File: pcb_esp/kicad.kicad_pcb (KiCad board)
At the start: 2 copper layers, 100 x 30 mm, 26 parts, among them J1 PRG, J2 SLP, J3 SHT21, J4 BH1750, J5 PWRIN, J6 GND, SW1 RST, SW2 PRG, U1 LT1963, U2 ESP-12F

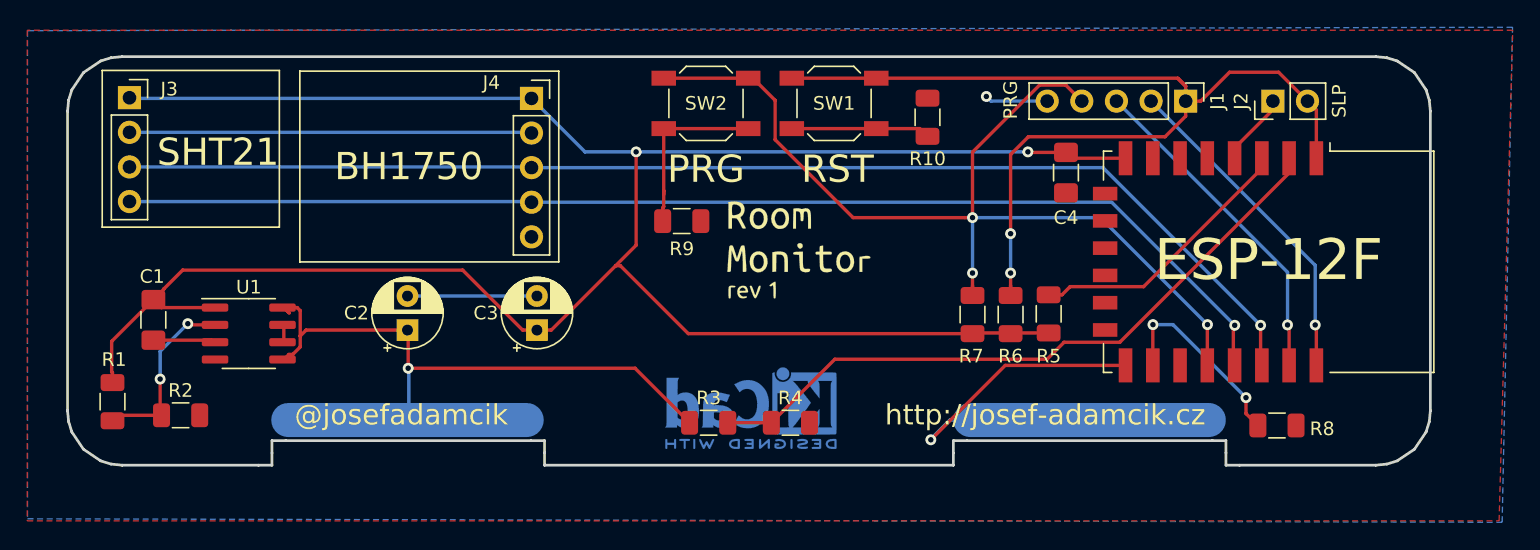
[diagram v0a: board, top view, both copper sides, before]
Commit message: Add GND connecting vias to the main PCB
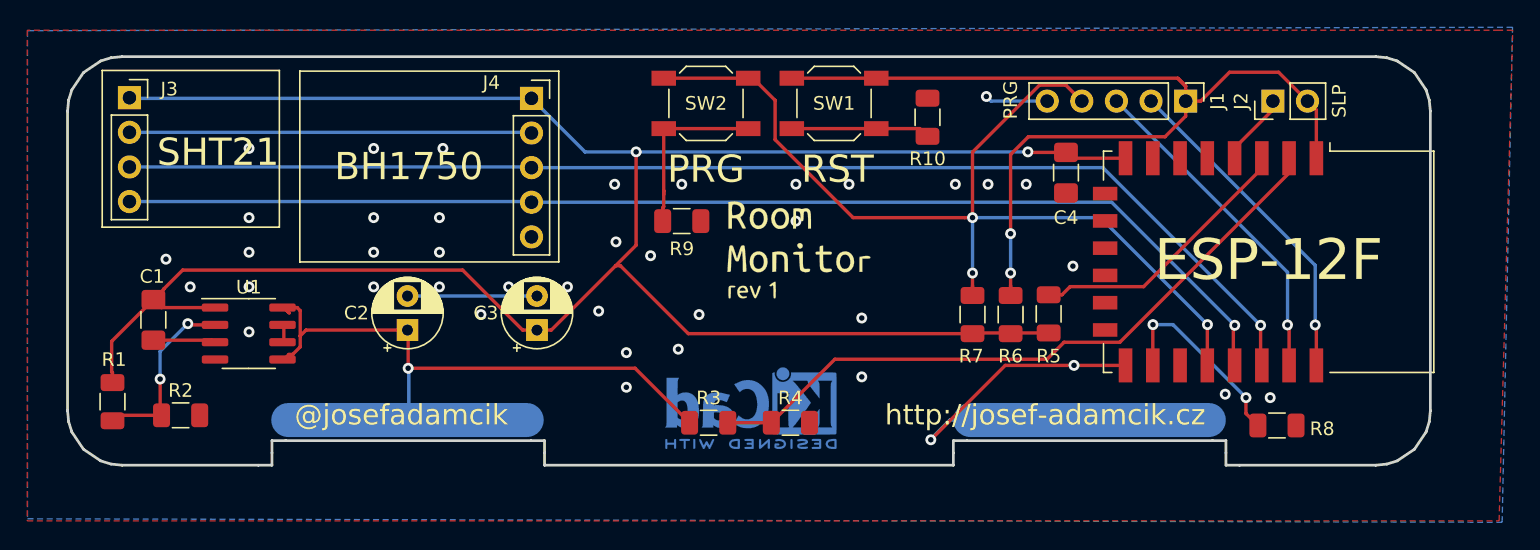
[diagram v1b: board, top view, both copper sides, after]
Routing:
- net GND: vias 2 -> 41
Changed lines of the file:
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@@
     (thickness 1.6)
     (drawings 61)
-    (tracks 181)
+    (tracks 221)
     (zones 0)
     (modules 26)
@@
   (page A4)
   (layers
-    (0 F.Cu signal)
+    (0 F.Cu signal hide)
     (31 B.Cu signal)
     (32 B.Adhes user)
@@
   (segment (start 94.95 46.6) (end 84.7 46.6) (width 0.25) (layer B.Cu) (net 3) (status 10))
   (segment (start 88.76 42.59) (end 83.3 48.05) (width 0.25) (layer F.Cu) (net 3))
-  (segment (start 97.59 42.59) (end 88.76 42.59) (width 0.25) (layer F.Cu) (net 3) (status 10))
+  (segment (start 97.59 42.59) (end 93.808 42.59) (width 0.25) (layer F.Cu) (net 3) (status 10))
   (via (at 87.376 22.86) (size 0.8) (drill 0.4) (layers F.Cu B.Cu) (net 3))
   (segment (start 87.716 23.2) (end 87.376 22.86) (width 0.25) (layer B.Cu) (net 3))
@@
   (segment (start 53.95 25.49) (end 54 25.54) (width 0.25) (layer B.Cu) (net 3))
   (segment (start 24.5 25.49) (end 53.95 25.49) (width 0.25) (layer B.Cu) (net 3))
+  (via (at 42.418 36.83) (size 0.8) (drill 0.4) (layers F.Cu B.Cu) (net 3))
+  (via (at 42.418 34.29) (size 0.8) (drill 0.4) (layers F.Cu B.Cu) (net 3))
+  (via (at 47.244 36.83) (size 0.8) (drill 0.4) (layers F.Cu B.Cu) (net 3))
+  (via (at 47.244 34.29) (size 0.8) (drill 0.4) (layers F.Cu B.Cu) (net 3))
+  (via (at 56.642 36.83) (size 0.8) (drill 0.4) (layers F.Cu B.Cu) (net 3))
+  (via (at 58.928 38.608) (size 0.8) (drill 0.4) (layers F.Cu B.Cu) (net 3))
+  (via (at 52.324 36.83) (size 0.8) (drill 0.4) (layers F.Cu B.Cu) (net 3))
+  (via (at 50.292 38.862) (size 0.8) (drill 0.4) (layers F.Cu B.Cu) (net 3))
+  (via (at 60.198 33.528) (size 0.8) (drill 0.4) (layers F.Cu B.Cu) (net 3))
+  (via (at 62.738 34.544) (size 0.8) (drill 0.4) (layers F.Cu B.Cu) (net 3))
+  (via (at 78.232 43.434) (size 0.8) (drill 0.4) (layers F.Cu B.Cu) (net 3))
+  (via (at 78.232 39.116) (size 0.8) (drill 0.4) (layers F.Cu B.Cu) (net 3))
+  (via (at 60.96 44.196) (size 0.8) (drill 0.4) (layers F.Cu B.Cu) (net 3))
+  (via (at 60.96 41.656) (size 0.8) (drill 0.4) (layers F.Cu B.Cu) (net 3))
+  (via (at 66.294 38.862) (size 0.8) (drill 0.4) (layers F.Cu B.Cu) (net 3))
+  (via (at 64.77 41.402) (size 0.8) (drill 0.4) (layers F.Cu B.Cu) (net 3))
+  (via (at 90.3 29.3) (size 0.8) (drill 0.4) (layers F.Cu B.Cu) (net 3))
+  (via (at 85.1 29.3) (size 0.8) (drill 0.4) (layers F.Cu B.Cu) (net 3))
+  (via (at 77.3 29.3) (size 0.8) (drill 0.4) (layers F.Cu B.Cu) (net 3))
+  (via (at 73.4 29.3) (size 0.8) (drill 0.4) (layers F.Cu B.Cu) (net 3))
+  (via (at 65.024 29.3) (size 0.8) (drill 0.4) (layers F.Cu B.Cu) (net 3))
+  (via (at 60.1 29.3) (size 0.8) (drill 0.4) (layers F.Cu B.Cu) (net 3))
+  (via (at 87.5 29.3) (size 0.8) (drill 0.4) (layers F.Cu B.Cu) (net 3))
+  (via (at 73.406 32.004) (size 0.8) (drill 0.4) (layers F.Cu B.Cu) (net 3))
+  (via (at 28.956 36.83) (size 0.8) (drill 0.4) (layers F.Cu B.Cu) (net 3))
+  (via (at 27.178 34.798) (size 0.8) (drill 0.4) (layers F.Cu B.Cu) (net 3))
+  (via (at 33.274 36.83) (size 0.8) (drill 0.4) (layers F.Cu B.Cu) (net 3))
+  (via (at 33.274 34.29) (size 0.8) (drill 0.4) (layers F.Cu B.Cu) (net 3))
+  (via (at 33.274 40.132) (size 0.8) (drill 0.4) (layers F.Cu B.Cu) (net 3))
+  (segment (start 93.808 42.59) (end 88.76 42.59) (width 0.25) (layer F.Cu) (net 3) (status 10))
+  (via (at 93.808 42.59) (size 0.8) (drill 0.4) (layers F.Cu B.Cu) (net 3))
+  (via (at 93.726 35.306) (size 0.8) (drill 0.4) (layers F.Cu B.Cu) (net 3))
+  (via (at 108.204 44.958) (size 0.8) (drill 0.4) (layers F.Cu B.Cu) (net 3))
+  (via (at 104.902 44.704) (size 0.8) (drill 0.4) (layers F.Cu B.Cu) (net 3))
+  (via (at 33.274 31.75) (size 0.8) (drill 0.4) (layers F.Cu B.Cu) (net 3))
+  (via (at 33.274 26.67) (size 0.8) (drill 0.4) (layers F.Cu B.Cu) (net 3))
+  (via (at 42.418 31.75) (size 0.8) (drill 0.4) (layers F.Cu B.Cu) (net 3))
+  (via (at 42.418 26.67) (size 0.8) (drill 0.4) (layers F.Cu B.Cu) (net 3))
+  (via (at 47.244 31.75) (size 0.8) (drill 0.4) (layers F.Cu B.Cu) (net 3))
+  (via (at 47.498 26.67) (size 0.8) (drill 0.4) (layers F.Cu B.Cu) (net 3))
   (via (at 86.36 35.814) (size 0.8) (drill 0.4) (layers F.Cu B.Cu) (net 4))
   (via (at 103.6 39.6) (size 0.8) (drill 0.4) (layers F.Cu B.Cu) (net 4))

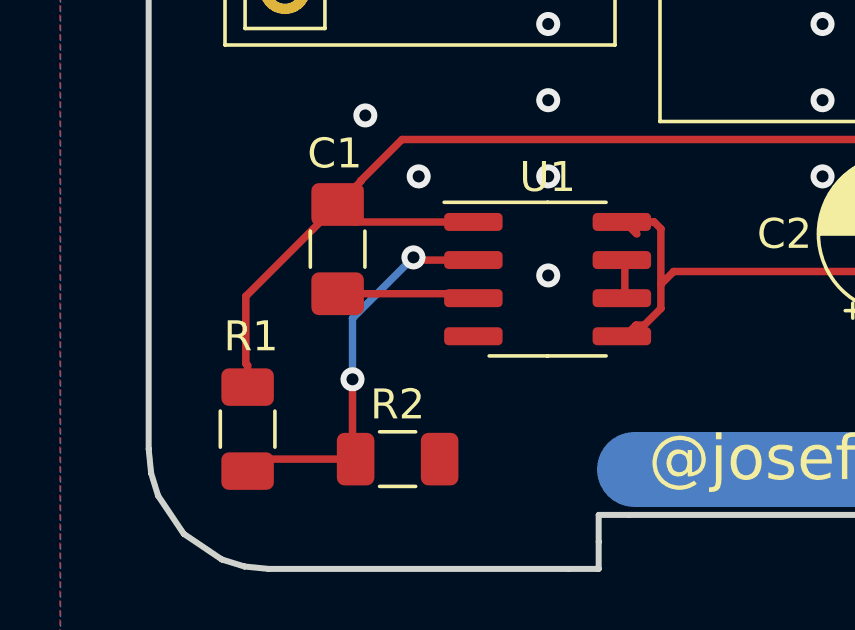
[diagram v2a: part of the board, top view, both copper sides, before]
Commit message: Fix lt1763 symbol (swapped gnd and byp pins) and fix pcb
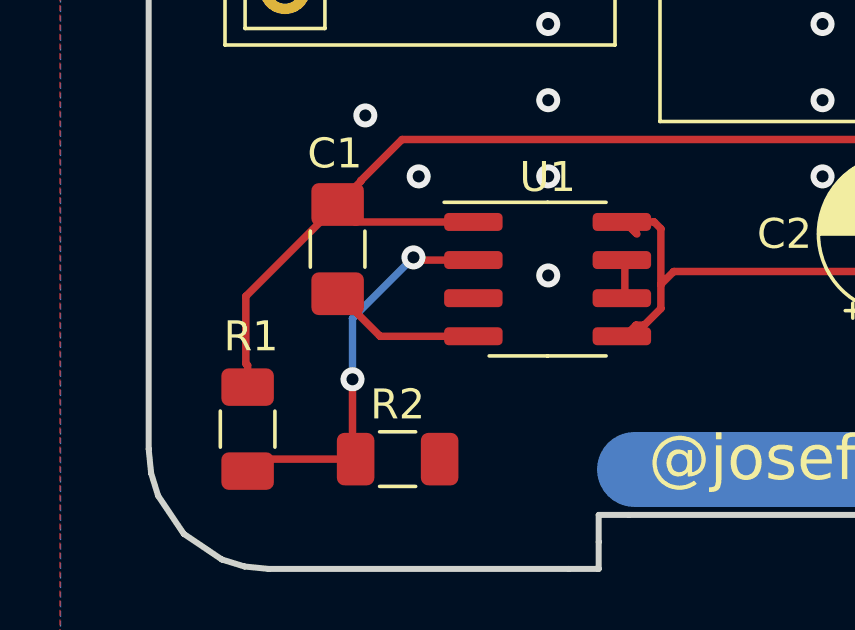
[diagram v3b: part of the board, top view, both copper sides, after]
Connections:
- J4 pad 5: (no net) -> Net-(J4-Pad5)
- U1 pad 3: /BYP -> GND
- U1 pad 4: GND -> /BYP
- U2 pad 10: (no net) -> Net-(U2-Pad10)
- U2 pad 11: (no net) -> Net-(U2-Pad11)
- U2 pad 12: (no net) -> Net-(U2-Pad12)
- U2 pad 13: (no net) -> Net-(U2-Pad13)
- U2 pad 14: (no net) -> Net-(U2-Pad14)
- U2 pad 17: (no net) -> Net-(U2-Pad17)
- U2 pad 5: (no net) -> Net-(U2-Pad5)
- U2 pad 6: (no net) -> Net-(U2-Pad6)
- U2 pad 7: (no net) -> Net-(U2-Pad7)
- U2 pad 9: (no net) -> Net-(U2-Pad9)
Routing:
- net /BYP: track 4.49 -> 5.11 mm
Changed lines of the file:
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@@
     (thickness 1.6)
     (drawings 61)
-    (tracks 221)
+    (tracks 222)
     (zones 0)
     (modules 26)
-    (nets 18)
+    (nets 29)
   )
   (page A4)
@@
   (net 16 /BYP)
   (net 17 /ADJ)
+  (net 18 "Net-(J4-Pad5)")
+  (net 19 "Net-(U2-Pad17)")
+  (net 20 "Net-(U2-Pad14)")
+  (net 21 "Net-(U2-Pad13)")
+  (net 22 "Net-(U2-Pad12)")
+  (net 23 "Net-(U2-Pad11)")
+  (net 24 "Net-(U2-Pad10)")
+  (net 25 "Net-(U2-Pad9)")
+  (net 26 "Net-(U2-Pad7)")
+  (net 27 "Net-(U2-Pad6)")
+  (net 28 "Net-(U2-Pad5)")
   (net_class Default "This is the default net class."
     (clearance 0.2)
@@
     (add_net DTR)
     (add_net GND)
+    (add_net "Net-(J4-Pad5)")
     (add_net "Net-(R10-Pad1)")
     (add_net "Net-(R9-Pad1)")
+    (add_net "Net-(U2-Pad10)")
+    (add_net "Net-(U2-Pad11)")
+    (add_net "Net-(U2-Pad12)")
+    (add_net "Net-(U2-Pad13)")
+    (add_net "Net-(U2-Pad14)")
+    (add_net "Net-(U2-Pad17)")
+    (add_net "Net-(U2-Pad5)")
+    (add_net "Net-(U2-Pad6)")
+    (add_net "Net-(U2-Pad7)")
+    (add_net "Net-(U2-Pad9)")
     (add_net PWR)
     (add_net RST)
@@
       (net 12 /PWR+))
     (pad 4 smd roundrect (at -2.475 1.905) (size 1.95 0.6) (layers F.Cu F.Paste F.Mask) (roundrect_rratio 0.25)
+      (net 16 /BYP))
+    (pad 3 smd roundrect (at -2.475 0.635) (size 1.95 0.6) (layers F.Cu F.Paste F.Mask) (roundrect_rratio 0.25)
       (net 3 GND))
-    (pad 3 smd roundrect (at -2.475 0.635) (size 1.95 0.6) (layers F.Cu F.Paste F.Mask) (roundrect_rratio 0.25)
-      (net 16 /BYP))
     (pad 2 smd roundrect (at -2.475 -0.635) (size 1.95 0.6) (layers F.Cu F.Paste F.Mask) (roundrect_rratio 0.25)
       (net 17 /ADJ))
@@
     (pad 18 smd rect (at 7.6 4.5 270) (size 2.5 1) (layers F.Cu F.Paste F.Mask)
       (net 4 DTR))
-    (pad 17 smd rect (at 7.6 6.5 270) (size 2.5 1) (layers F.Cu F.Paste F.Mask))
+    (pad 17 smd rect (at 7.6 6.5 270) (size 2.5 1) (layers F.Cu F.Paste F.Mask)
+      (net 19 "Net-(U2-Pad17)"))
     (pad 16 smd rect (at 7.6 8.5 270) (size 2.5 1) (layers F.Cu F.Paste F.Mask)
       (net 15 /GPIO15))
     (pad 15 smd rect (at 7.6 10.5 270) (size 2.5 1) (layers F.Cu F.Paste F.Mask)
       (net 3 GND))
-    (pad 14 smd rect (at 5 12 270) (size 1 1.8) (layers F.Cu F.Paste F.Mask))
-    (pad 13 smd rect (at 3 12 270) (size 1 1.8) (layers F.Cu F.Paste F.Mask))
-    (pad 12 smd rect (at 1 12 270) (size 1 1.8) (layers F.Cu F.Paste F.Mask))
-    (pad 11 smd rect (at -1 12 270) (size 1 1.8) (layers F.Cu F.Paste F.Mask))
-    (pad 10 smd rect (at -3 12 270) (size 1 1.8) (layers F.Cu F.Paste F.Mask))
-    (pad 9 smd rect (at -5 12 270) (size 1 1.8) (layers F.Cu F.Paste F.Mask))
+    (pad 14 smd rect (at 5 12 270) (size 1 1.8) (layers F.Cu F.Paste F.Mask)
+      (net 20 "Net-(U2-Pad14)"))
+    (pad 13 smd rect (at 3 12 270) (size 1 1.8) (layers F.Cu F.Paste F.Mask)
+      (net 21 "Net-(U2-Pad13)"))
+    (pad 12 smd rect (at 1 12 270) (size 1 1.8) (layers F.Cu F.Paste F.Mask)
+      (net 22 "Net-(U2-Pad12)"))
+    (pad 11 smd rect (at -1 12 270) (size 1 1.8) (layers F.Cu F.Paste F.Mask)
+      (net 23 "Net-(U2-Pad11)"))
+    (pad 10 smd rect (at -3 12 270) (size 1 1.8) (layers F.Cu F.Paste F.Mask)
+      (net 24 "Net-(U2-Pad10)"))
+    (pad 9 smd rect (at -5 12 270) (size 1 1.8) (layers F.Cu F.Paste F.Mask)
+      (net 25 "Net-(U2-Pad9)"))
     (pad 8 smd rect (at -7.6 10.5 270) (size 2.5 1) (layers F.Cu F.Paste F.Mask)
       (net 2 PWR))
-    (pad 7 smd rect (at -7.6 8.5 270) (size 2.5 1) (layers F.Cu F.Paste F.Mask))
-    (pad 6 smd rect (at -7.6 6.5 270) (size 2.5 1) (layers F.Cu F.Paste F.Mask))
-    (pad 5 smd rect (at -7.6 4.5 270) (size 2.5 1) (layers F.Cu F.Paste F.Mask))
+    (pad 7 smd rect (at -7.6 8.5 270) (size 2.5 1) (layers F.Cu F.Paste F.Mask)
+      (net 26 "Net-(U2-Pad7)"))
+    (pad 6 smd rect (at -7.6 6.5 270) (size 2.5 1) (layers F.Cu F.Paste F.Mask)
+      (net 27 "Net-(U2-Pad6)"))
+    (pad 5 smd rect (at -7.6 4.5 270) (size 2.5 1) (layers F.Cu F.Paste F.Mask)
+      (net 28 "Net-(U2-Pad5)"))
     (pad 4 smd rect (at -7.6 2.5 270) (size 2.5 1) (layers F.Cu F.Paste F.Mask)
       (net 13 /GPIO16))
@@
     (fp_line (start 0.635 -1.27) (end 1.27 -0.635) (layer F.Fab) (width 0.1))
     (fp_line (start -1.27 -1.27) (end 0.635 -1.27) (layer F.Fab) (width 0.1))
-    (pad 5 thru_hole oval (at 0 10.16) (size 1.7 1.7) (drill 1) (layers *.Cu *.Mask))
+    (pad 5 thru_hole oval (at 0 10.16) (size 1.7 1.7) (drill 1) (layers *.Cu *.Mask)
+      (net 18 "Net-(J4-Pad5)"))
     (pad 4 thru_hole oval (at 0 7.62) (size 1.7 1.7) (drill 1) (layers *.Cu *.Mask)
       (net 10 SDA))
@@
   (segment (start 106.426 46.126) (end 107.3 47) (width 0.25) (layer F.Cu) (net 15) (status 20))
   (segment (start 106.426 44.958) (end 106.426 46.126) (width 0.25) (layer F.Cu) (net 15))
-  (segment (start 30.5315 40.7415) (end 30.679 40.889) (width 0.25) (layer F.Cu) (net 16) (status 30))
-  (segment (start 26.254 40.7415) (end 30.5315 40.7415) (width 0.25) (layer F.Cu) (net 16) (status 30))
+  (segment (start 30.5315 40.7415) (end 30.679 40.889) (width 0.25) (layer F.Cu) (net 3) (status 30))
+  (segment (start 27.6715 42.159) (end 30.779 42.159) (width 0.25) (layer F.Cu) (net 16))
+  (segment (start 26.254 40.7415) (end 27.6715 42.159) (width 0.25) (layer F.Cu) (net 16))
   (via (at 26.75 43.594) (size 0.8) (drill 0.4) (layers F.Cu B.Cu) (net 17))
   (via (at 28.782 39.53) (size 0.8) (drill 0.4) (layers F.Cu B.Cu) (net 17))
